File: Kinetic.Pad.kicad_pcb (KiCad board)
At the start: 2 copper layers, 57.2 x 67.1 mm, 21 parts, among them SW1 Rotary_Encoder_Switch, U1 ProMicro

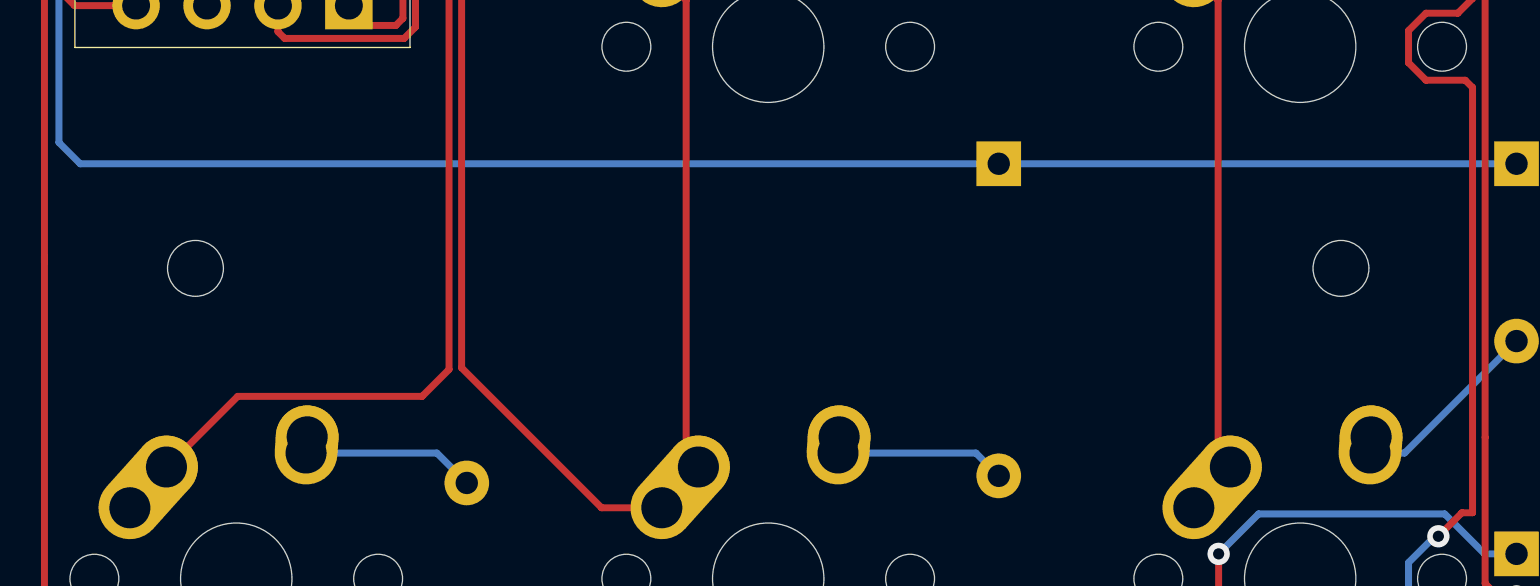
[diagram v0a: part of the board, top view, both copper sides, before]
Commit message: Updated MX Libraries
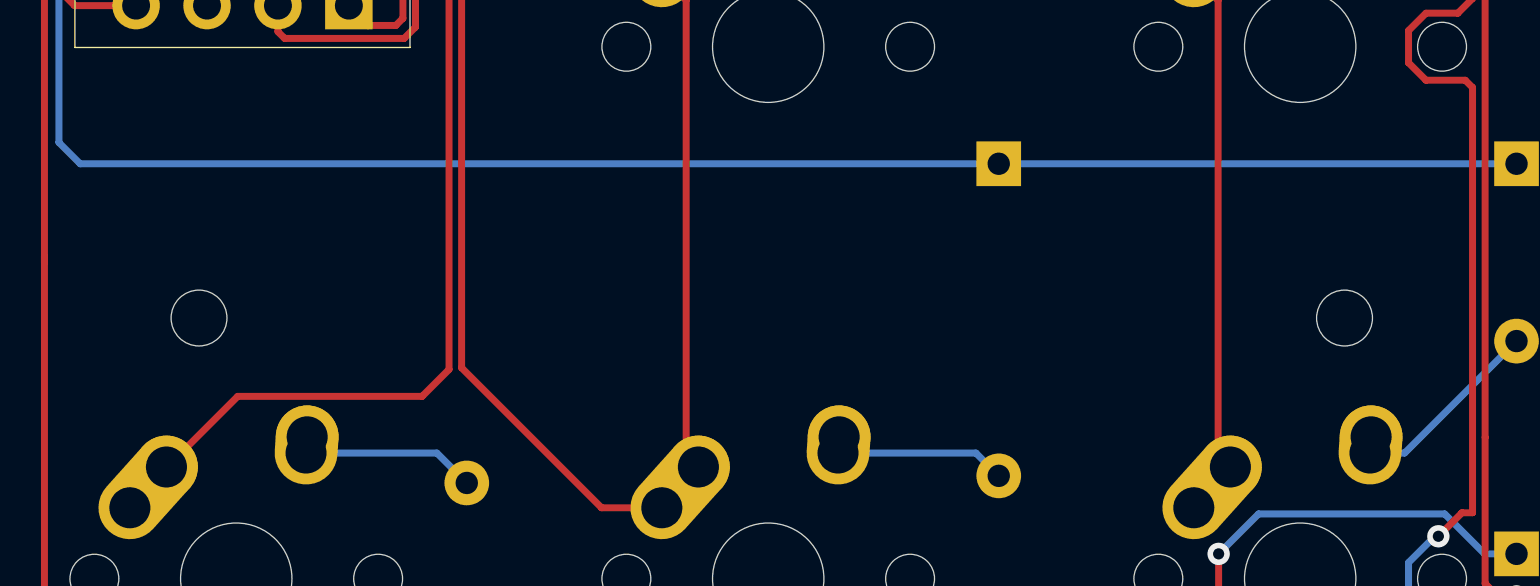
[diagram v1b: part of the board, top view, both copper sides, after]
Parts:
- moved ? 1.78 mm to (258.1, 66.9)
- moved ? 1.78 mm to (217.1, 66.9)

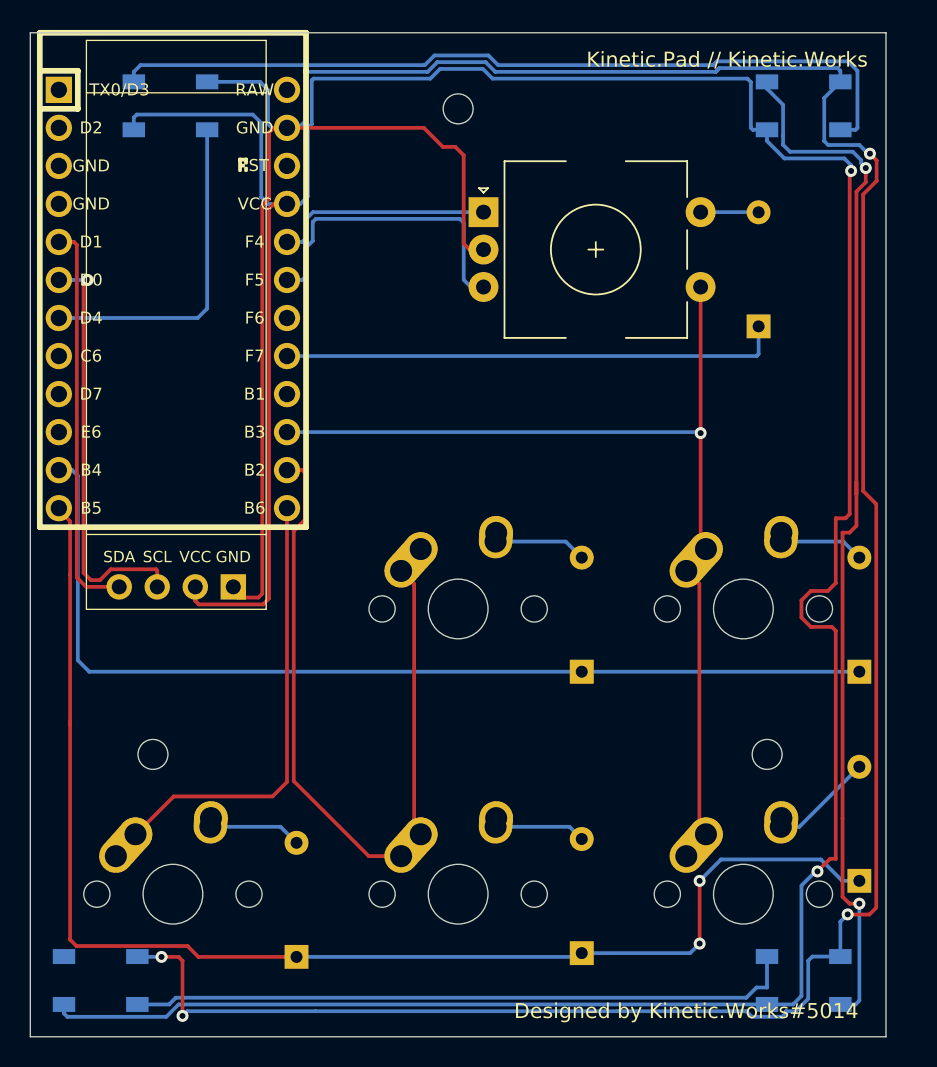
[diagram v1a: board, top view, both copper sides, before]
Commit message: Switched Libraries, Deleted Old Gerbers, Deleted Old Step FIle
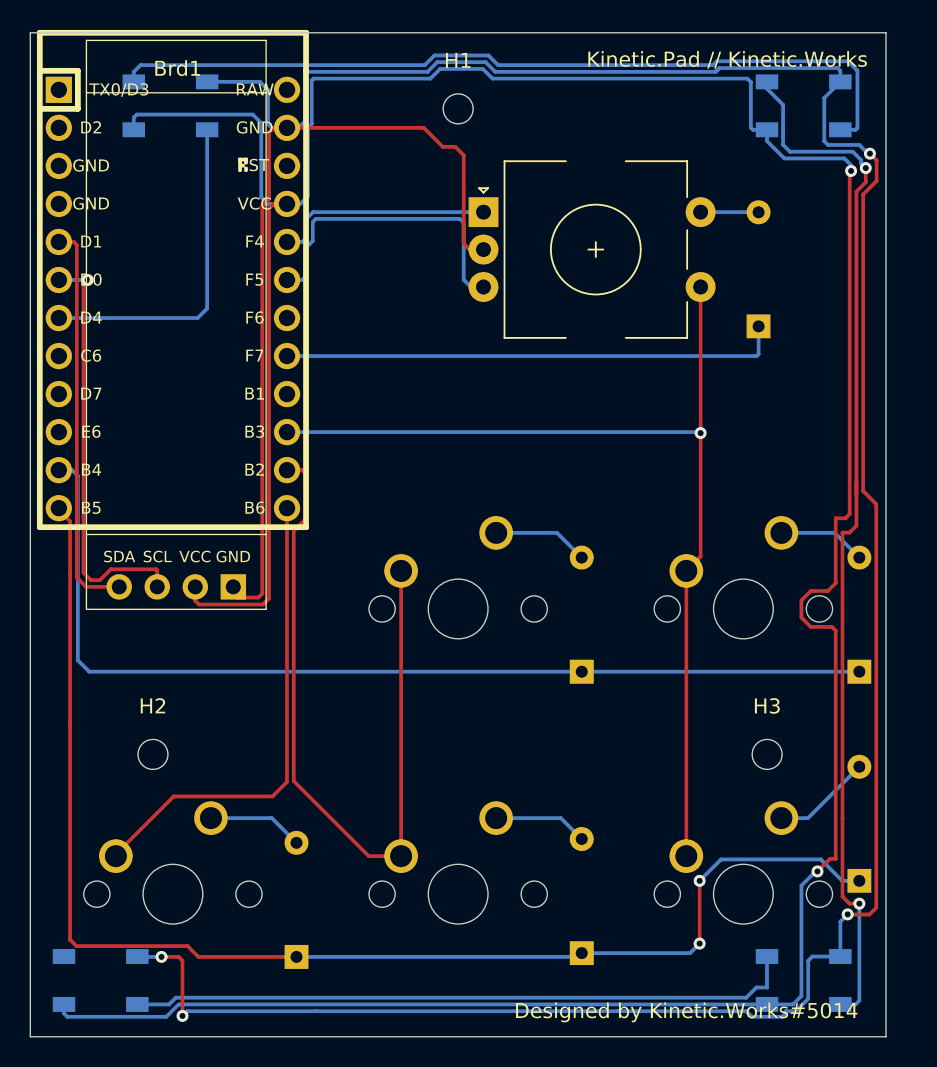
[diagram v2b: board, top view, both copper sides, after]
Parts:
- MX1, MX2, MX3, MX4, MX5: footprint MX_Alps_Hybrid:MX-1U-NoLED -> MX_Only:MXOnly-1U-NoLED
- gave numbers to parts that had none: 14
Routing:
- net C2: track 51.2 -> 50.5 mm
- net C3: track 66.8 -> 66.1 mm

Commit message: Removed Old Gerbers
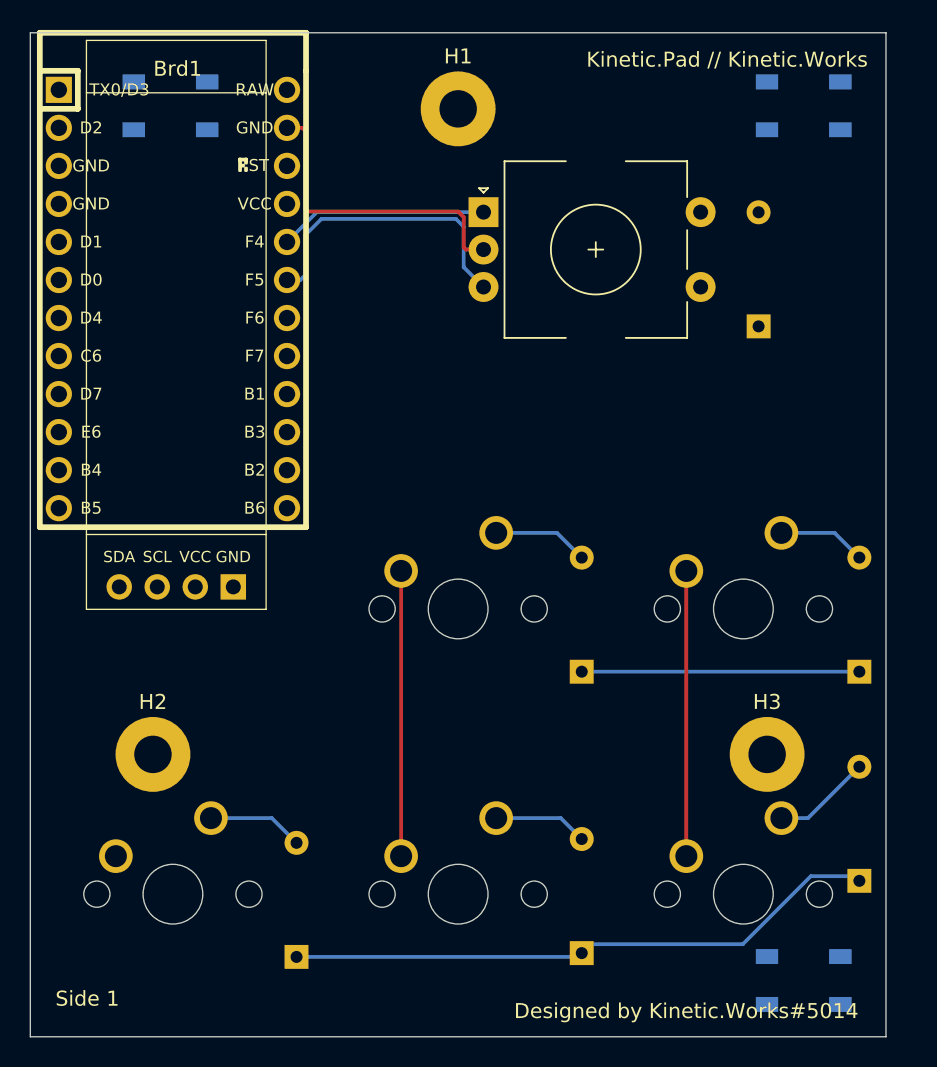
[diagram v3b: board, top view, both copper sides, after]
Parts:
- removed D10: WS2812B, LED_SMD:LED_WS2812B_PLCC4_5.0x5.0mm_P3.2mm
- H1, H2, H3: value MountingHole -> MountingHole_Pad; footprint MountingHole:MountingHole_2mm -> MountingHole:MountingHole_2.5mm_Pad
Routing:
- net +5V: track 212.4 -> 0.00 mm, vias 2 -> 0
- net GND: track 224.5 -> 20.7 mm, vias 4 -> 0
- net Net-(D2-Pad2): track 70.5 -> 0.00 mm, vias 2 -> 0
- net Net-(D1-Pad2): track 55.1 -> 0.00 mm
- net R3: track 88.3 -> 40.0 mm, vias 2 -> 0
- net R2: track 66.3 -> 18.5 mm
- net C3: track 66.1 -> 20.8 mm, vias 1 -> 0
- net Net-(D4-Pad2): track 44.6 -> 0.00 mm
- net R1: track 33.4 -> 0.00 mm
- net C1: track 31.8 -> 0.00 mm
- net C2: track 50.5 -> 19.0 mm
- net SCL: track 28.2 -> 0.00 mm, vias 1 -> 0
- net SDA: track 26.6 -> 0.00 mm
- net DIN: track 22.1 -> 0.00 mm
- net Net-(D7-Pad2): track 3.88 -> 0.00 mm
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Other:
- board text added: "Side 1"
- board text added: "Side 2"

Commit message: Nightly Files
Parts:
- removed D1, D2, D4: WS2812B, LED_SMD:LED_WS2812B_PLCC4_5.0x5.0mm_P3.2mm
- moved D9 4.83 mm to (264.3, 80.1)
- renumbered Brd1 to OLED
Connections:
- U1 pad 1: Net-(U1-Pad1) -> unconnected-(U1-Pad1)
- U1 pad 10: Net-(U1-Pad10) -> unconnected-(U1-Pad10)
- U1 pad 16: Net-(U1-Pad16) -> unconnected-(U1-Pad16)
- U1 pad 18: Net-(U1-Pad18) -> unconnected-(U1-Pad18)
- U1 pad 2: Net-(U1-Pad2) -> unconnected-(U1-Pad2)
- U1 pad 22: Net-(U1-Pad22) -> unconnected-(U1-Pad22)
- U1 pad 24: Net-(U1-Pad24) -> unconnected-(U1-Pad24)
- U1 pad 8: Net-(U1-Pad8) -> unconnected-(U1-Pad8)
- U1 pad 9: Net-(U1-Pad9) -> unconnected-(U1-Pad9)
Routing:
- net GND: track 20.7 -> 109.1 mm, vias 0 -> 1
- net R2: track 18.5 -> 66.5 mm
- net C3: track 20.8 -> 65.1 mm, vias 0 -> 1
- net R3: track 40.0 -> 83.3 mm, vias 0 -> 1
- net C1: track 0.00 -> 34.0 mm
- net R1: track 0.00 -> 33.2 mm
- net +5V: track 0.00 -> 31.5 mm
- net SDA: track 0.00 -> 28.9 mm, vias 0 -> 1
- net SCL: track 0.00 -> 26.8 mm
- net C2: track 19.0 -> 33.2 mm
- net B: track 19.9 -> 13.3 mm
- net A: track 13.9 -> 18.3 mm
- net Net-(D7-Pad2): track 0.00 -> 3.88 mm
- net Net-(D8-Pad2): track 5.89 -> 6.62 mm
- net Net-(D5-Pad2): track 6.40 -> 7.13 mm
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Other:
- net class Default removed
